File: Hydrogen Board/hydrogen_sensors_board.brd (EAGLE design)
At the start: 68.2 x 66 mm, 42 parts, among them U1 ATMEGA328P_TQFP, Y1 16MHz

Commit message: update
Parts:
- removed F3, F4: (no value), polyfuse:1206
- removed U$4: RJ9PTH, SparkFun-Connectors:RJ9
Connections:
- removed net N$12: F3.1, U$4.4
- removed net N$14: F4.1, U$4.3
- net +12V: now also ETH1.P$6; no longer F3.2
- net +5V: now also ETH1.P$8; no longer F4.2
- net GND: no longer U$4.1, U$4.2
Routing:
- net GND: track 321.9 -> 281.6 mm
- net N$14: track 27.2 -> 0.00 mm
- net +12V: track 29.3 -> 55.5 mm
- net +5V: track 194.3 -> 186.4 mm, vias 4 -> 5
- net N$12: track 5.74 -> 0.00 mm
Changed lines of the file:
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@@
 <setting verticaltext="up"/>
 </settings>
-<grid distance="0.05" unitdist="inch" unit="inch" style="lines" multiple="1" display="yes" altdistance="0.005" altunitdist="inch" altunit="inch"/>
+<grid distance="0.025" unitdist="inch" unit="inch" style="lines" multiple="1" display="yes" altdistance="0.005" altunitdist="inch" altunit="inch"/>
 <layers>
 <layer number="1" name="Top" color="4" fill="1" visible="yes" active="yes"/>
@@
 <attribute name="NAME" x="2.54" y="30.988" size="1.016" layer="26" ratio="21" rot="MR180"/>
 </element>
-<element name="U$4" library="SparkFun-Connectors" package="RJ9" value="RJ9PTH" x="41.91" y="11.43" smashed="yes"/>
-<element name="F3" library="polyfuse" package="1206" value="" x="45.72" y="26.67" smashed="yes" rot="MR90">
-<attribute name="NAME" x="46.863" y="25.4" size="1.016" layer="26" ratio="21" rot="MR90"/>
-<attribute name="VALUE" x="44.196" y="25.273" size="0.4064" layer="28" rot="MR90"/>
-</element>
-<element name="F4" library="polyfuse" package="1206" value="" x="17.78" y="11.43" smashed="yes" rot="R180">
-<attribute name="NAME" x="19.05" y="10.287" size="1.016" layer="25" ratio="21" rot="R180"/>
-<attribute name="VALUE" x="19.177" y="12.954" size="0.4064" layer="27" rot="R180"/>
-</element>
 <element name="C3" library="adafruit" package="C0603" value="" x="30.48" y="27.94" smashed="yes">
 <attribute name="NAME" x="29.591" y="28.702" size="1.016" layer="25" ratio="21"/>
@@
 <via x="21.59" y="33.02" extent="1-16" drill="0.6"/>
 <wire x1="21.59" y1="33.02" x2="21.59" y2="31.35" width="0.254" layer="1"/>
-<wire x1="46.57" y1="31.75" x2="46.57" y2="39.37" width="0.254" layer="1"/>
+<wire x1="46.57" y1="31.75" x2="46.57" y2="33.655" width="0.254" layer="1"/>
+<wire x1="46.57" y1="33.655" x2="46.57" y2="39.37" width="0.254" layer="1"/>
 <wire x1="7.5438" y1="35.1028" x2="7.5438" y2="24.13" width="0.254" layer="16"/>
 <wire x1="3.6576" y1="38.989" x2="7.5438" y2="35.1028" width="0.254" layer="16"/>
@@
 <wire x1="7.5438" y1="24.13" x2="7.747" y2="24.13" width="0.254" layer="16"/>
 <wire x1="5.0292" y1="44.2468" x2="5.08" y2="44.45" width="0.254" layer="16"/>
-<contactref element="F4" pad="2"/>
 <contactref element="C3" pad="1"/>
 <contactref element="C4" pad="1"/>
@@
 <contactref element="C7" pad="1"/>
 <contactref element="C8" pad="1"/>
-<wire x1="61.7575" y1="19.5225" x2="61.7575" y2="21.4775" width="0.254" layer="16"/>
-<wire x1="61.7575" y1="21.4775" x2="63.14" y2="22.86" width="0.254" layer="16"/>
-<wire x1="63.14" y1="22.86" x2="63.14" y2="24.815" width="0.254" layer="16"/>
-<wire x1="63.14" y1="24.815" x2="61.7575" y2="26.1975" width="0.254" layer="16"/>
-<wire x1="61.7575" y1="26.1975" x2="61.4325" y2="26.1975" width="0.254" layer="1"/>
-<wire x1="61.4325" y1="26.1975" x2="57.15" y2="30.48" width="0.254" layer="1"/>
-<wire x1="57.15" y1="30.48" x2="48.26" y2="30.48" width="0.254" layer="1"/>
-<wire x1="48.26" y1="30.48" x2="46.99" y2="31.75" width="0.254" layer="1"/>
-<wire x1="46.99" y1="31.75" x2="46.57" y2="31.75" width="0.254" layer="1"/>
 <wire x1="46.57" y1="31.75" x2="46.57" y2="31.076" width="0.254" layer="1"/>
 <wire x1="46.57" y1="31.076" x2="45.466" y2="29.972" width="0.254" layer="1"/>
 <wire x1="45.466" y1="29.972" x2="41.822" y2="29.972" width="0.254" layer="1"/>
 <wire x1="41.822" y1="29.972" x2="39.79" y2="27.94" width="0.254" layer="1"/>
-<wire x1="16.38" y1="11.43" x2="16.51" y2="11.43" width="0.254" layer="1"/>
-<wire x1="16.38" y1="11.43" x2="15.24" y2="11.43" width="0.254" layer="1"/>
-<wire x1="15.24" y1="11.43" x2="11.43" y2="15.24" width="0.254" layer="1"/>
-<wire x1="11.43" y1="15.24" x2="11.43" y2="20.447" width="0.254" layer="1"/>
-<wire x1="11.43" y1="20.447" x2="7.747" y2="24.13" width="0.254" layer="1"/>
 <wire x1="39.79" y1="24.13" x2="39.79" y2="27.94" width="0.254" layer="1"/>
 <wire x1="34.71" y1="24.13" x2="34.71" y2="27.94" width="0.254" layer="1"/>
@@
 <via x="34.29" y="21.59" extent="1-16" drill="0.6"/>
 <wire x1="34.29" y1="21.59" x2="33.23" y2="22.65" width="0.254" layer="1"/>
+<contactref element="ETH1" pad="P$8"/>
+<wire x1="57.91" y1="39.62" x2="57.91" y2="38.86" width="1.016" layer="16"/>
+<wire x1="57.91" y1="38.86" x2="55.88" y2="36.83" width="1.016" layer="16"/>
+<wire x1="55.88" y1="36.83" x2="55.88" y2="32.075" width="1.016" layer="16"/>
+<wire x1="55.88" y1="32.075" x2="61.7575" y2="26.1975" width="1.016" layer="16"/>
+<wire x1="61.7575" y1="26.1975" x2="61.7575" y2="24.2425" width="1.016" layer="16"/>
+<wire x1="61.7575" y1="24.2425" x2="63.14" y2="22.86" width="1.016" layer="16"/>
+<wire x1="63.14" y1="22.86" x2="63.14" y2="20.905" width="1.016" layer="16"/>
+<wire x1="63.14" y1="20.905" x2="61.7575" y2="19.5225" width="1.016" layer="16"/>
+<wire x1="55.88" y1="32.075" x2="49.84" y2="32.075" width="1.016" layer="16"/>
+<wire x1="49.84" y1="32.075" x2="48.26" y2="33.655" width="1.016" layer="16"/>
+<via x="48.26" y="33.655" extent="1-16" drill="0.6" shape="square"/>
+<wire x1="48.26" y1="33.655" x2="46.57" y2="33.655" width="1.016" layer="1"/>
 </signal>
 <signal name="GND">
@@
 <wire x1="5.2578" y1="39.2176" x2="6.4008" y2="39.2176" width="0.254" layer="1"/>
 <wire x1="5.2578" y1="39.2176" x2="5.08" y2="39.37" width="0.254" layer="1"/>
-<contactref element="U$4" pad="2"/>
-<contactref element="U$4" pad="1"/>
 <contactref element="C8" pad="2"/>
 <contactref element="C7" pad="2"/>
@@
 <wire x1="21.59" y1="11.43" x2="21.59" y2="14.19" width="0.254" layer="16"/>
 <wire x1="21.59" y1="14.19" x2="22.86" y2="15.46" width="0.254" layer="16"/>
-<wire x1="40.005" y1="17.78" x2="40.005" y2="19.05" width="0.254" layer="1"/>
-<wire x1="40.005" y1="19.05" x2="41.275" y2="20.32" width="0.254" layer="1"/>
-<wire x1="53.7" y1="22.86" x2="42.76" y2="22.86" width="0.254" layer="1"/>
-<wire x1="42.76" y1="22.86" x2="41.49" y2="24.13" width="0.254" layer="1"/>
-<wire x1="42.76" y1="22.86" x2="42.76" y2="21.805" width="0.254" layer="1"/>
-<wire x1="42.76" y1="21.805" x2="41.275" y2="20.32" width="0.254" layer="1"/>
 <wire x1="30.94" y1="11.94" x2="30.94" y2="13.16" width="0.254" layer="16"/>
 <wire x1="30.94" y1="13.16" x2="33.02" y2="15.24" width="0.254" layer="16"/>
 <wire x1="33.02" y1="15.24" x2="33.02" y2="18.034" width="0.254" layer="16"/>
 <wire x1="33.02" y1="18.034" x2="33.147" y2="18.161" width="0.254" layer="16"/>
-<wire x1="33.147" y1="18.161" x2="39.624" y2="18.161" width="0.254" layer="1"/>
-<wire x1="39.624" y1="18.161" x2="40.005" y2="17.78" width="0.254" layer="1"/>
-<wire x1="41.49" y1="27.94" x2="41.49" y2="22.44" width="0.254" layer="1"/>
-<wire x1="41.49" y1="22.44" x2="40.64" y2="21.59" width="0.254" layer="1"/>
-<wire x1="40.64" y1="21.59" x2="39.37" y2="21.59" width="0.254" layer="1"/>
-<wire x1="39.37" y1="21.59" x2="38.1" y2="20.32" width="0.254" layer="1"/>
-<wire x1="38.1" y1="20.32" x2="36.83" y2="21.59" width="0.254" layer="1"/>
-<wire x1="36.83" y1="21.59" x2="36.83" y2="23.71" width="0.254" layer="1"/>
-<wire x1="36.83" y1="23.71" x2="36.41" y2="24.13" width="0.254" layer="1"/>
 <polygon width="0.4064" layer="1" isolate="0.3048">
 <vertex x="0" y="0"/>
@@
 <contactref element="JP4" pad="3"/>
 <contactref element="H_INPUT" pad="3"/>
-<contactref element="F3" pad="2"/>
 <wire x1="24.94" y1="11.94" x2="24.94" y2="12.24" width="0.254" layer="16"/>
 <wire x1="24.94" y1="12.24" x2="27.94" y2="15.24" width="0.254" layer="16"/>
 <wire x1="27.94" y1="15.24" x2="27.94" y2="18.034" width="0.254" layer="16"/>
 <wire x1="27.94" y1="18.034" x2="28.067" y2="18.161" width="0.254" layer="16"/>
-<wire x1="37.9476" y1="28.0416" x2="45.72" y2="28.0416" width="0.254" layer="16"/>
-<wire x1="28.067" y1="18.161" x2="37.9476" y2="28.0416" width="0.254" layer="16"/>
-<wire x1="45.72" y1="28.0416" x2="45.72" y2="28.07" width="0.254" layer="16"/>
+<contactref element="ETH1" pad="P$6"/>
+<wire x1="57.91" y1="41.66" x2="56.9" y2="41.66" width="1.016" layer="1"/>
+<wire x1="56.9" y1="41.66" x2="55.245" y2="40.005" width="1.016" layer="1"/>
+<wire x1="55.245" y1="40.005" x2="55.245" y2="35.56" width="1.016" layer="1"/>
+<wire x1="55.245" y1="35.56" x2="53.34" y2="33.655" width="1.016" layer="1"/>
+<wire x1="53.34" y1="33.655" x2="51.435" y2="33.655" width="1.016" layer="1"/>
+<wire x1="51.435" y1="33.655" x2="44.45" y2="26.67" width="1.016" layer="1"/>
+<wire x1="44.45" y1="26.67" x2="44.45" y2="22.86" width="1.016" layer="1"/>
+<wire x1="44.45" y1="22.86" x2="36.83" y2="15.24" width="1.016" layer="1"/>
+<wire x1="36.83" y1="15.24" x2="29.21" y2="15.24" width="1.016" layer="1"/>
+<wire x1="29.21" y1="15.24" x2="27.94" y2="16.51" width="1.016" layer="1"/>
+<wire x1="27.94" y1="16.51" x2="27.94" y2="18.034" width="1.016" layer="1"/>
+<wire x1="27.94" y1="18.034" x2="28.067" y2="18.161" width="1.016" layer="1"/>
 </signal>
 <signal name="N$10">
@@
 <wire x1="59.56" y1="52.07" x2="58.8" y2="51.31" width="0.254" layer="16"/>
 </signal>
-<signal name="N$12">
-<contactref element="U$4" pad="4"/>
-<contactref element="F3" pad="1"/>
-<wire x1="43.815" y1="20.32" x2="43.815" y2="23.365" width="0.254" layer="16"/>
-<wire x1="43.815" y1="23.365" x2="45.72" y2="25.27" width="0.254" layer="16"/>
-</signal>
-<signal name="N$14">
-<contactref element="U$4" pad="3"/>
-<contactref element="F4" pad="1"/>
-<wire x1="19.18" y1="11.43" x2="19.05" y2="11.43" width="0.254" layer="1"/>
-<wire x1="19.18" y1="11.43" x2="21.59" y2="11.43" width="0.254" layer="1"/>
-<wire x1="21.59" y1="11.43" x2="22.86" y2="10.16" width="0.254" layer="1"/>
-<wire x1="22.86" y1="10.16" x2="33.02" y2="10.16" width="0.254" layer="1"/>
-<wire x1="33.02" y1="10.16" x2="36.83" y2="13.97" width="0.254" layer="1"/>
-<wire x1="36.83" y1="13.97" x2="38.735" y2="13.97" width="0.254" layer="1"/>
-<wire x1="38.735" y1="13.97" x2="42.545" y2="17.78" width="0.254" layer="1"/>
-</signal>
 </signals>

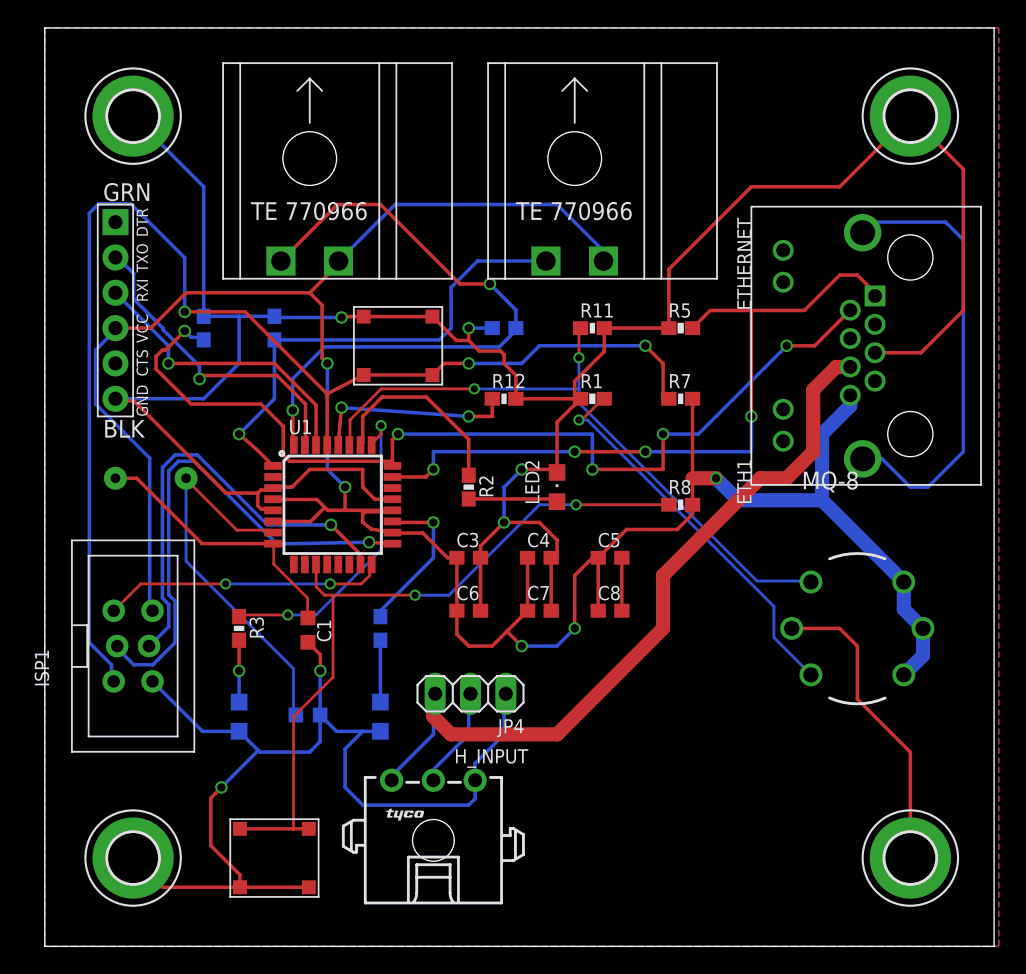
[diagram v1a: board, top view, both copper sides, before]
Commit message: cleaned up silk screens
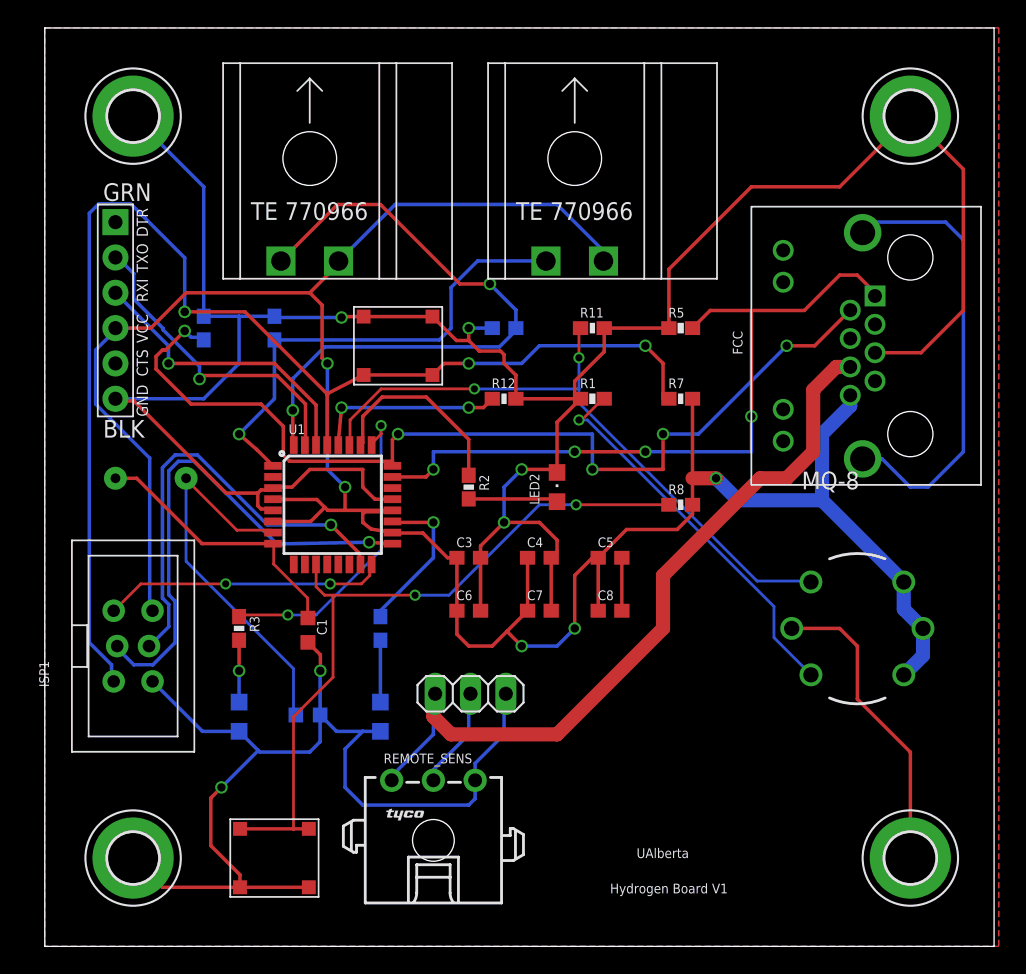
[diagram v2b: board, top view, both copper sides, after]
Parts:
- ETH1: value ETHERNET -> FCC
- renumbered H_INPUT to REMOTE_SENS
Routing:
- net H2OUT_2: track 14.8 -> 13.8 mm
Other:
- board text added: "Hydrogen Board V1"
- board text added: "UAlberta"
